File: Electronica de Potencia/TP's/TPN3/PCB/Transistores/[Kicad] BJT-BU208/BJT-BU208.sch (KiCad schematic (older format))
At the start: 26 parts, among them J1 Vin, J2 PWM_IN, Q1 BC548, Q2 BC558, Q3 BU208, U1 L7812, U2 L7905

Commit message: Arreglo placa de potencia
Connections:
- net -5V: now also Q2.1 (C); no longer Q2.3 (E)
- net at D1.1 (K), JP1.3, Q3.2 (B)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: now also Q2.3 (E); no longer Q2.1 (C)
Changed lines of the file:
@@
 F 3 "http://www.redrok.com/PNP_BC327_-45V_-800mA_0.625W_Hfe100_TO-92.pdf" H 6300 5225 50  0001 L CNN
 	1    6300 5225
-	1    0    0    -1
+	1    0    0    1
 $EndComp
 $Comp

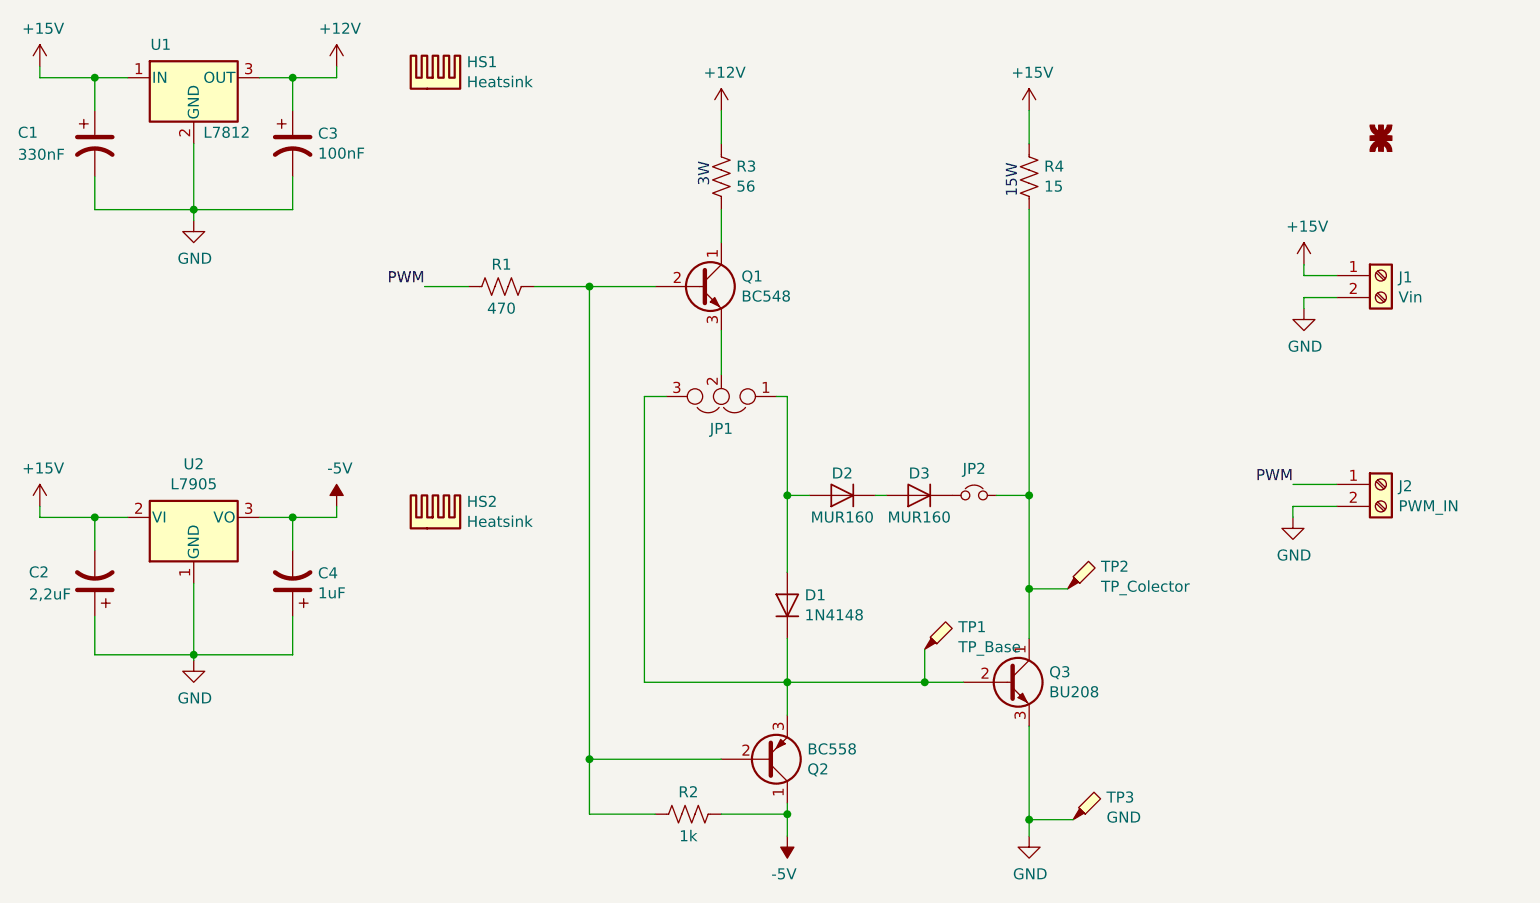
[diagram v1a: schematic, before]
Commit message: Arreglo placa BJT potencia
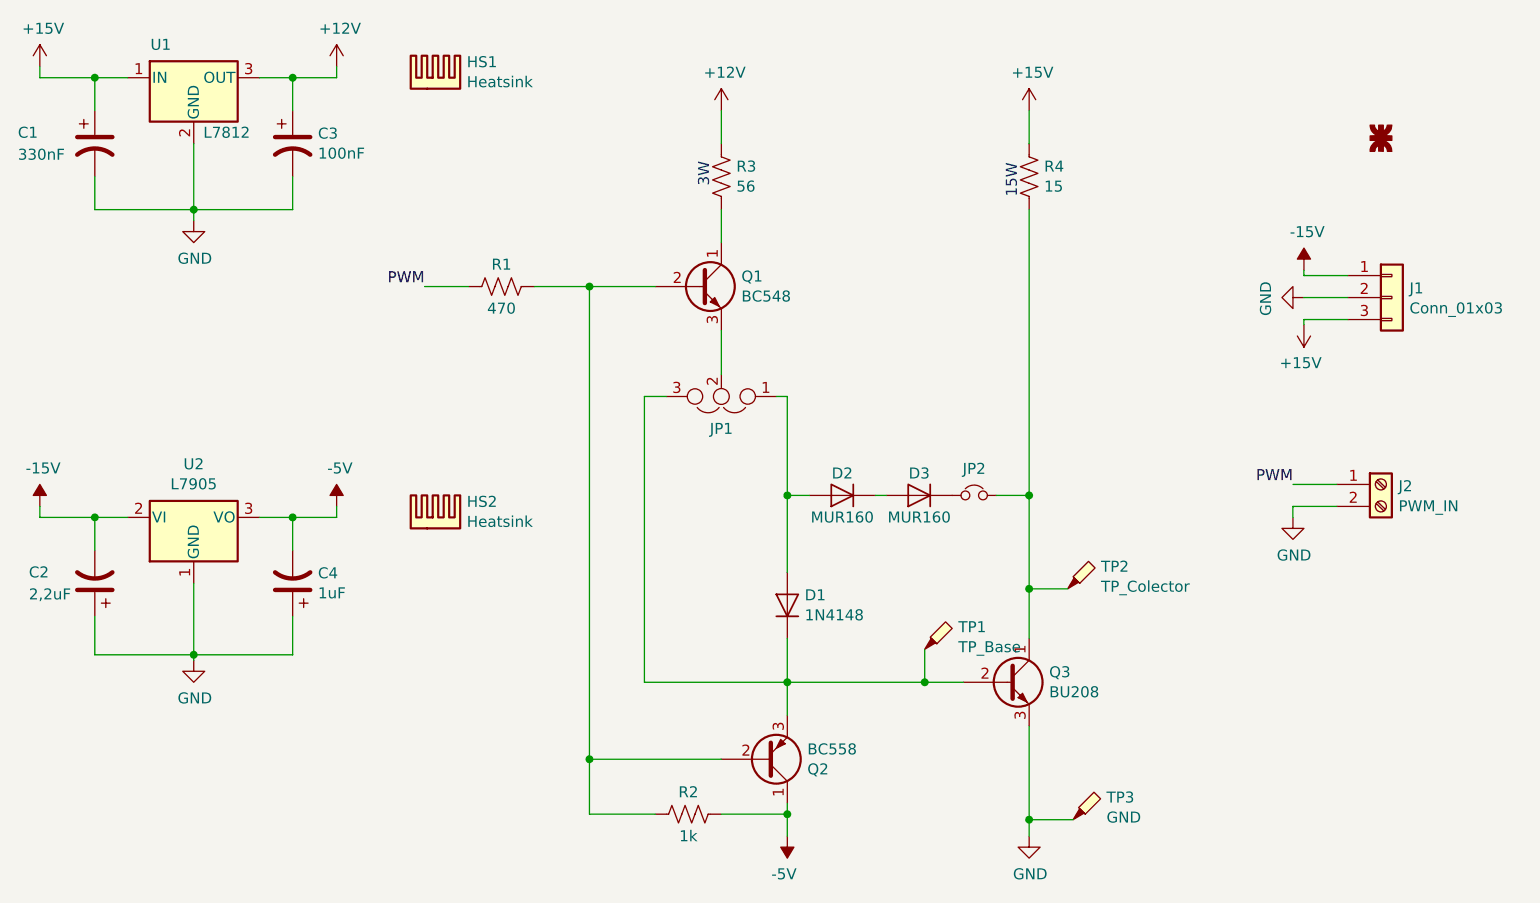
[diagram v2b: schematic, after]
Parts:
- removed J1: Vin, lib_fp:TerminalBlock_bornier-2_P5.08mm, symbol BJT-BU208:Screw_Terminal_01x02
- added J1: Conn_01x03, lib_fp:TerminalBlock_bornier-3_P5.08mm, symbol BJT-BU208:Conn_01x03
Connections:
- net +15V: now also J1.3 (Pin_3); no longer C2.2, U2.2 (VI)
- net GND: now also J1.2 (Pin_2)
- new net -15V: C2.2, J1.1 (Pin_1), U2.2 (VI)
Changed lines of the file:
@@
-$EndComp
-$Comp
-L BJT-BU208:Screw_Terminal_01x02 J1
-U 1 1 5CD853EA
-P 9100 3025
-F 0 "J1" H 9180 3017 50  0000 L CNN
-F 1 "Vin" H 9180 2926 50  0000 L CNN
-F 2 "lib_fp:TerminalBlock_bornier-2_P5.08mm" H 9100 3025 50  0001 C CNN
-F 3 "~" H 9100 3025 50  0001 C CNN
-	1    9100 3025
-	1    0    0    -1
 $EndComp
 $Comp
@@
 L BJT-BU208:+15V #PWR012
 U 1 1 5CD8D783
-P 8750 2975
-F 0 "#PWR012" H 8750 2825 50  0001 C CNN
-F 1 "+15V" H 8765 3148 50  0000 C CNN
-F 2 "" H 8750 2975 50  0001 C CNN
-F 3 "" H 8750 2975 50  0001 C CNN
-	1    8750 2975
-	1    0    0    -1
-$EndComp
-Wire Wire Line
-	8900 3025 8750 3025
-Wire Wire Line
-	8750 3025 8750 2975
+P 8750 3250
+F 0 "#PWR012" H 8750 3100 50  0001 C CNN
+F 1 "+15V" H 8765 3423 50  0000 C CNN
+F 2 "" H 8750 3250 50  0001 C CNN
+F 3 "" H 8750 3250 50  0001 C CNN
+	1    8750 3250
+	-1   0    0    1
+$EndComp
+Wire Wire Line
+	8950 3025 8750 3025
+Wire Wire Line
+	8750 3025 8750 3000
 $Comp
 L BJT-BU208:GND #PWR013
 U 1 1 5CD8DC20
-P 8750 3175
-F 0 "#PWR013" H 8750 2925 50  0001 C CNN
-F 1 "GND" H 8755 3002 50  0000 C CNN
-F 2 "" H 8750 3175 50  0001 C CNN
-F 3 "" H 8750 3175 50  0001 C CNN
-	1    8750 3175
-	1    0    0    -1
-$EndComp
-Wire Wire Line
-	8750 3175 8750 3125
-Wire Wire Line
-	8750 3125 8900 3125
+P 8750 3125
+F 0 "#PWR013" H 8750 2875 50  0001 C CNN
+F 1 "GND" H 8755 2952 50  0000 C CNN
+F 2 "" H 8750 3125 50  0001 C CNN
+F 3 "" H 8750 3125 50  0001 C CNN
+	1    8750 3125
+	0    1    1    0
+$EndComp
+Wire Wire Line
+	8750 3125 8950 3125
 $Comp
 L BJT-BU208:+15V #PWR01
@@
 	1    0    0    -1
 $EndComp
-$Comp
-L BJT-BU208:+15V #PWR02
-U 1 1 5CD9CB8F
-P 3000 4075
-F 0 "#PWR02" H 3000 3925 50  0001 C CNN
-F 1 "+15V" H 3015 4248 50  0000 C CNN
-F 2 "" H 3000 4075 50  0001 C CNN
-F 3 "" H 3000 4075 50  0001 C CNN
-	1    3000 4075
-	1    0    0    -1
-$EndComp
 Wire Wire Line
 	3000 4075 3000 4125
 Wire Wire Line
 	3000 4125 3250 4125
-Wire Wire Line
-	3250 4275 3250 4125
 Connection ~ 3250 4125
 Wire Wire Line
@@
 Wire Wire Line
 	3250 4750 3250 4575
+$Comp
+L BJT-BU208:-15V #PWR02
+U 1 1 5CF6272A
+P 3000 4075
+F 0 "#PWR02" H 3000 4175 50  0001 C CNN
+F 1 "-15V" H 3015 4248 50  0000 C CNN
+F 2 "" H 3000 4075 50  0001 C CNN
+F 3 "" H 3000 4075 50  0001 C CNN
+	1    3000 4075
+	1    0    0    -1
+$EndComp
+$Comp
+L BJT-BU208:Conn_01x03 J1
+U 1 1 5CF6363B
+P 9150 3125
+F 0 "J1" H 9230 3167 50  0000 L CNN
+F 1 "Conn_01x03" H 9230 3076 50  0000 L CNN
+F 2 "lib_fp:TerminalBlock_bornier-3_P5.08mm" H 9150 3125 50  0001 C CNN
+F 3 "~" H 9150 3125 50  0001 C CNN
+	1    9150 3125
+	1    0    0    -1
+$EndComp
+$Comp
+L power:-15V #PWR014
+U 1 1 5CF63A69
+P 8750 3000
+F 0 "#PWR014" H 8750 3100 50  0001 C CNN
+F 1 "-15V" H 8765 3173 50  0000 C CNN
+F 2 "" H 8750 3000 50  0001 C CNN
+F 3 "" H 8750 3000 50  0001 C CNN
+	1    8750 3000
+	1    0    0    -1
+$EndComp
+Wire Wire Line
+	8750 3250 8750 3225
+Wire Wire Line
+	8750 3225 8950 3225
+Wire Wire Line
+	3250 4125 3250 4275
 $EndSCHEMATC
